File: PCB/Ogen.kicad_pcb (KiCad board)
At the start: 2 copper layers, 28 x 21.5 mm, 19 parts, among them J1 Input, U1 PMW3360DM-T2QU, U2 AP2127K-ADJ, U3 TXS0102DCU, U4 TXS0102DCU, U5 TXS0102DCU

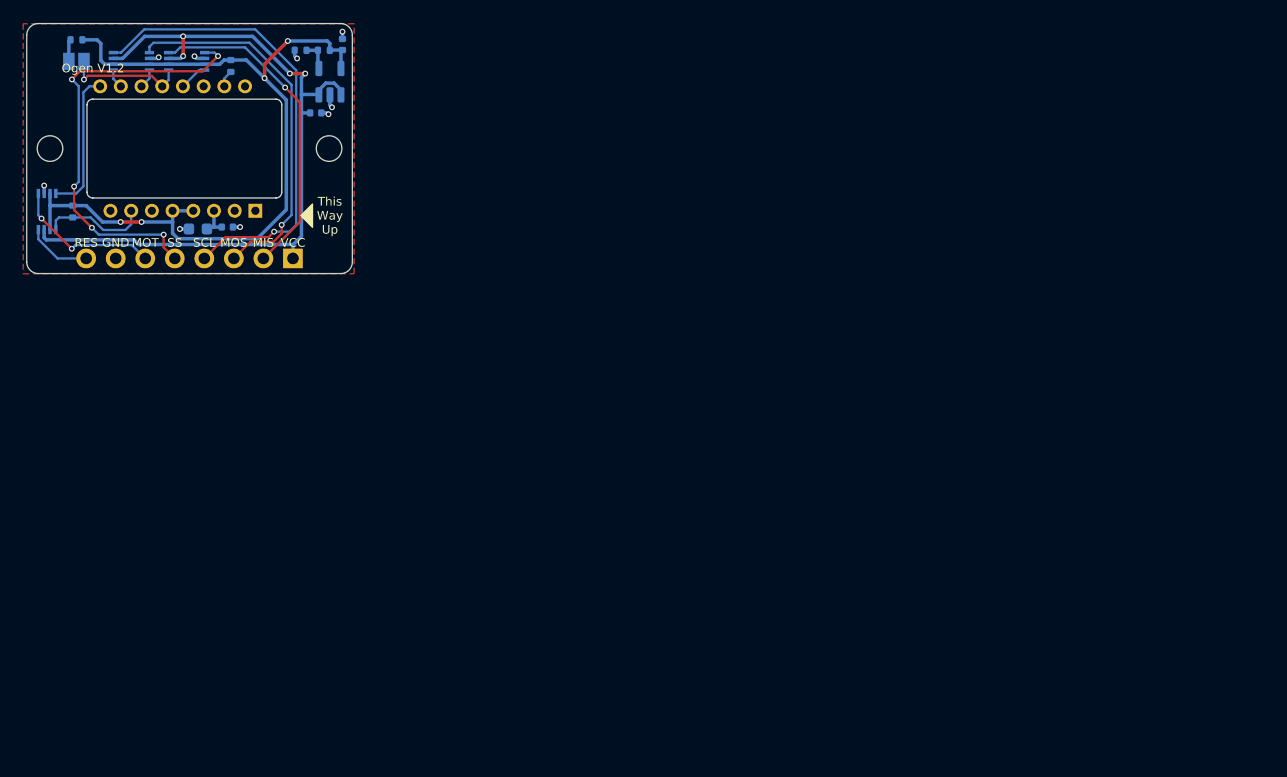
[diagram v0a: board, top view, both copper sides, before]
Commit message: 04/08/2023 update
Updated to V1.3. Changed all parts back to 0603. Stitched ground planes together. Removed MISO pullup jumper (MISO is pulled up by default now). Added metadata to schematic and PCB file. Changed location of production files for easier access.
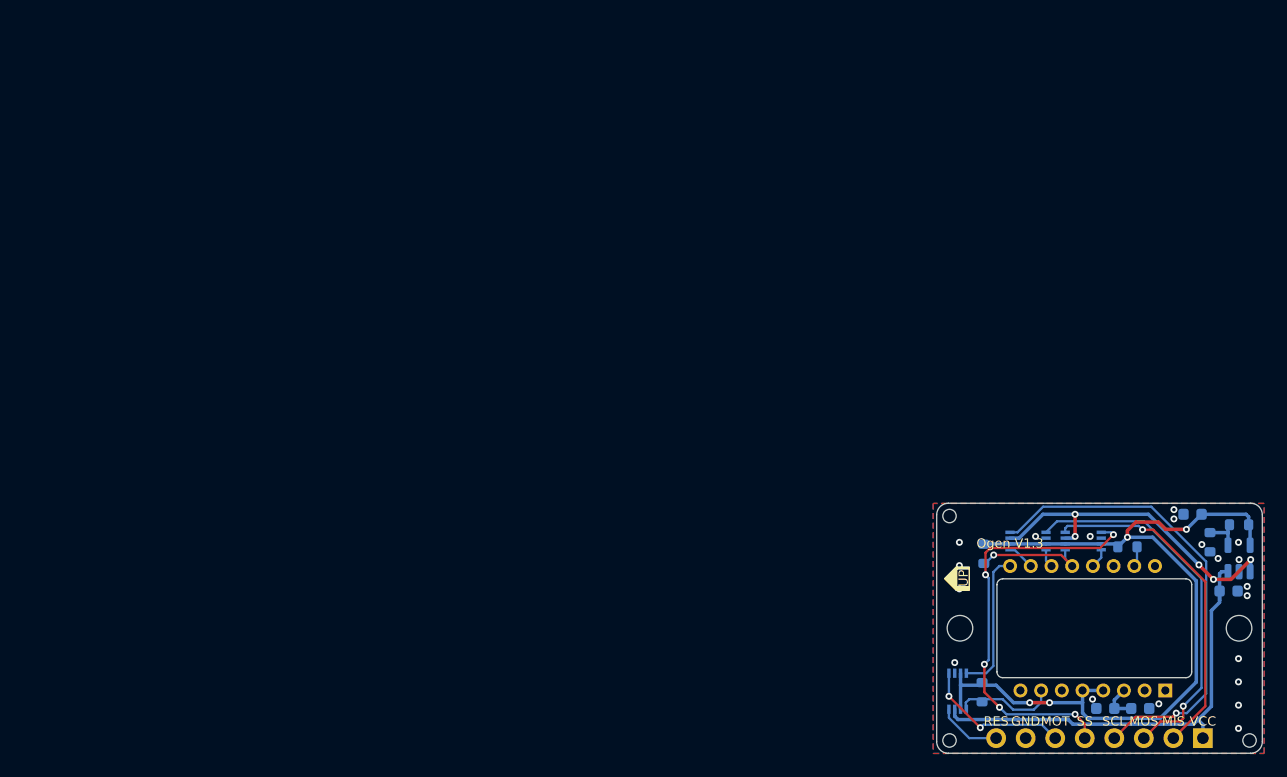
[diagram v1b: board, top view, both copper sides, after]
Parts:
- removed JP1: Jumper, Jumper:SolderJumper-2_P1.3mm_Open_Pad1.0x1.5mm
- added H3: Tooling Hole, Ogen:JLC Tooling Hole, F.Cu at (92.1, 55.4)
- added H4: Tooling Hole, Ogen:JLC Tooling Hole, F.Cu at (92.1, 74.7)
- added H5: Tooling Hole, Ogen:JLC Tooling Hole, F.Cu at (117.9, 74.7)
- C2, C3, C4: footprint Capacitor_SMD:C_0402_1005Metric -> Capacitor_SMD:C_0603_1608Metric
- R1, R2, R3, R4, R5: footprint Resistor_SMD:R_0402_1005Metric -> Resistor_SMD:R_0603_1608Metric
- U3, U4, U5: footprint Package_SO:VSSOP-8_2.3x2mm_P0.5mm -> Ogen:VSSOP-8_2.3x2mm_P0.5mm
- moved C1 90.9 mm to (108.5, 71.9), turned to 0 degrees
- moved R2 89.7 mm to (95.0, 58.6), turned to -90 degrees
- moved R4 88.9 mm to (114.5, 57.6), turned to -90 degrees
- moved A1 88.9 mm to (97.3, 55.8)
- moved R5 88.6 mm to (117.0, 56.1)
- moved C3 88.6 mm to (116.1, 61.8)
- moved U3 88.5 mm to (92.8, 70.4)
- moved H1 88.5 mm to (117.0, 65.0)
- moved H2 88.5 mm to (93.0, 65.0)
- moved J1 88.5 mm to (105.0, 74.5)
- moved U1 88.5 mm to (105.0, 65.0)
- moved R1 88.5 mm to (94.9, 70.5)
- moved U2 88.3 mm to (117.0, 59.0)
- moved R3 87.5 mm to (107.4, 58.0), turned to 180 degrees
- moved U4 87.4 mm to (98.8, 57.5)
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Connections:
- R2 pad 2: Net-(JP1-A) -> MISO
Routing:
- net GND: track 7.09 -> 0.00 mm, vias 9 -> 20
- net +2V: track 70.2 -> 72.9 mm
- net Net-(JP1-A): track 1.92 -> 0.00 mm
- net SS-H: track 37.8 -> 36.0 mm
- net VCC: track 65.9 -> 67.6 mm, vias 4 -> 5
- net MISO-H: track 28.1 -> 29.1 mm
- net Net-(U2-ADJ): track 2.58 -> 3.37 mm
- net SS: track 2.45 -> 1.70 mm
- net SCLK: track 1.67 -> 2.37 mm
- net MISO: track 10.4 -> 9.82 mm
- net Net-(U1-VDDPIX): track 2.76 -> 3.34 mm
- added copper zone on B.Cu, net GND
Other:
- board text added: "Ogen V1.3"
- board text added: "UP"
- board text removed: "MISO Pullup"
- board text removed: "Ogen V1.2"
- board text removed: "This Way Up"

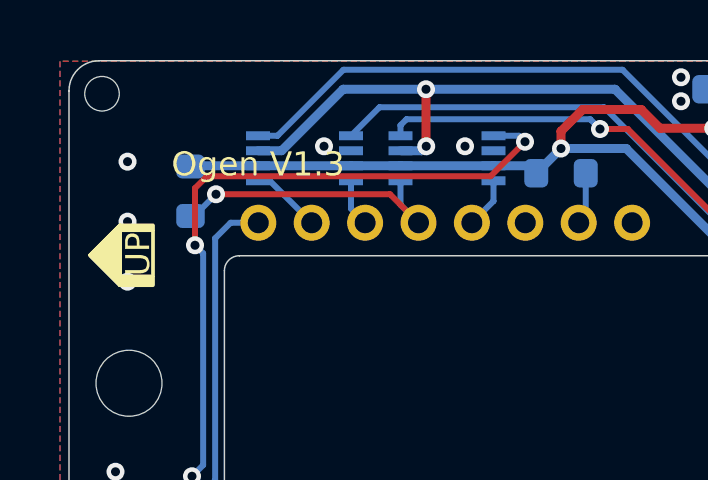
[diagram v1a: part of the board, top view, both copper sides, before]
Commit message: 18/09/2023 update
Updated to V1.4. Fixed .gitignore file. Changed LDO capacitors to 4u7 to match the one used in the PMW3360.
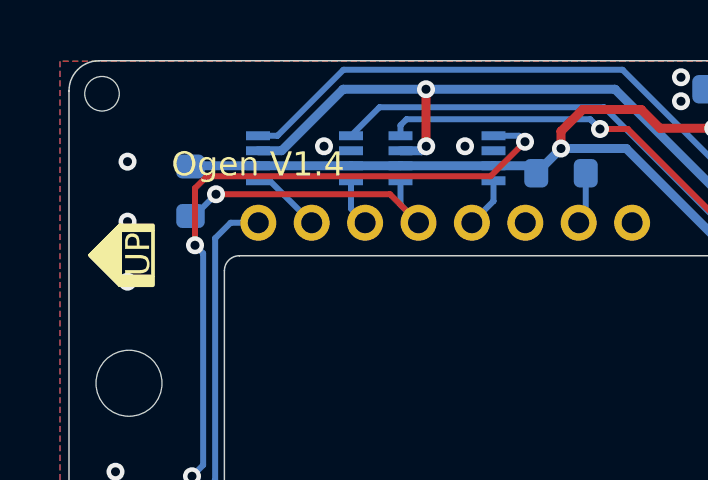
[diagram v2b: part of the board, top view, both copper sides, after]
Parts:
- C3, C4: value 1u -> 4u7
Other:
- board text added: "Ogen V1.4"
- board text removed: "Ogen V1.3"
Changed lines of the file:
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@@
   (title_block
     (title "Ogen PMW3360 Module")
-    (date "2023-08-04")
-    (rev "V1.3")
-    (company "Created by Ariamelon (https://github.com/Ariamelon/Ogen/tree/V1.3)")
+    (date "2023-09-18")
+    (rev "V1.4")
+    (company "Created by Ariamelon (https://github.com/Ariamelon/Ogen/tree/V1)")
     (comment 1 "Licensed under CC BY 4.0.")
   )
@@
     (property "Sheetfile" "Ogen.kicad_sch")
     (property "Sheetname" "")
+    (property "Voltage" "16V")
     (property "ki_description" "Unpolarized capacitor, small symbol")
     (property "ki_keywords" "capacitor cap")
@@
     (tags "capacitor")
     (property "Description" "0603 capacitor")
-    (property "LCSC" "C15849")
-    (property "Sheetfile" "Ogen.kicad_sch")
-    (property "Sheetname" "")
+    (property "LCSC" "C19666")
+    (property "Sheetfile" "Ogen.kicad_sch")
+    (property "Sheetname" "")
+    (property "Voltage" "16V")
     (property "ki_description" "Unpolarized capacitor, small symbol")
     (property "ki_keywords" "capacitor cap")
@@
         (effects (font (size 0.8 0.8) (thickness 0.1)) (justify mirror))
     )
-    (fp_text value "1u" (at 0 -1.43 180 unlocked) (layer "B.Fab")
+    (fp_text value "4u7" (at 0 -1.43 180 unlocked) (layer "B.Fab")
         (effects (font (size 1 1) (thickness 0.15)) (justify mirror))
     )
@@
     (tags "capacitor")
     (property "Description" "0603 capacitor")
-    (property "LCSC" "C15849")
-    (property "Sheetfile" "Ogen.kicad_sch")
-    (property "Sheetname" "")
+    (property "LCSC" "C19666")
+    (property "Sheetfile" "Ogen.kicad_sch")
+    (property "Sheetname" "")
+    (property "Voltage" "16V")
     (property "ki_description" "Unpolarized capacitor, small symbol")
     (property "ki_keywords" "capacitor cap")
@@
         (effects (font (size 0.8 0.8) (thickness 0.1)) (justify mirror))
     )
-    (fp_text value "1u" (at 0 -1.43 unlocked) (layer "B.Fab")
+    (fp_text value "4u7" (at 0 -1.43 unlocked) (layer "B.Fab")
         (effects (font (size 1 1) (thickness 0.15)) (justify mirror))
     )
@@
     (effects (font (size 0.8 0.8) (thickness 0.1)))
   )
-  (gr_text "Ogen V1.3" (at 97.3 57.7) (layer "F.SilkS")
+  (gr_text "Ogen V1.4" (at 97.3 57.7) (layer "F.SilkS")
     (effects (font (size 0.8 0.8) (thickness 0.1)))
   )

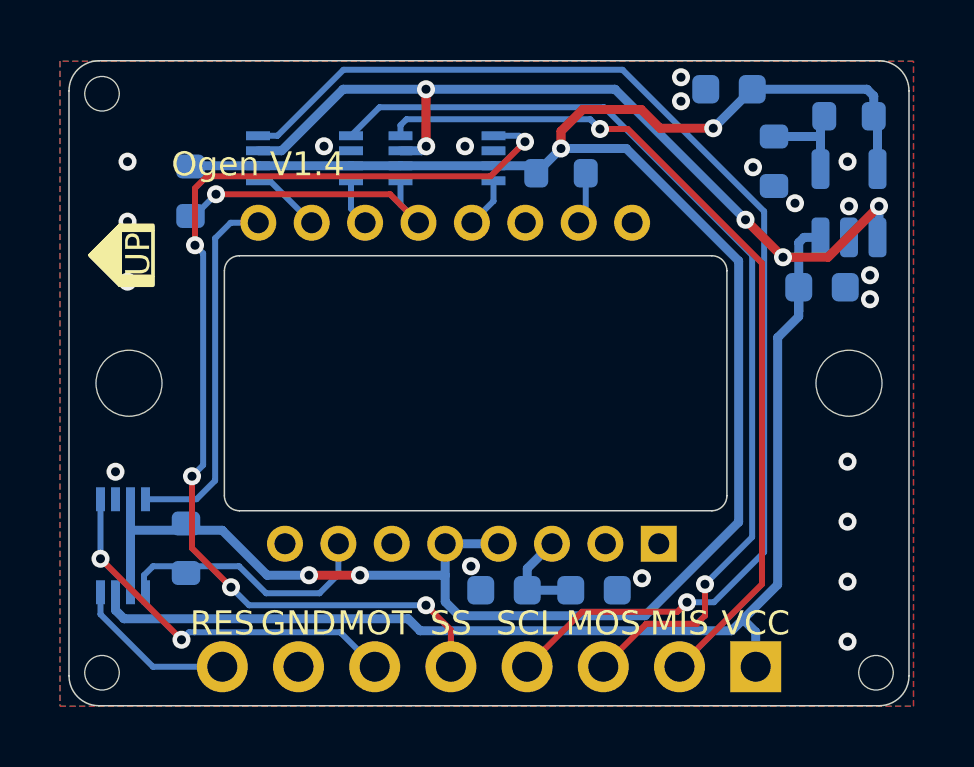
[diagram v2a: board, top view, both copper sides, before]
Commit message: V1.5 update
Changed LDO to XC6206P202MR. Unified libraries with master library.
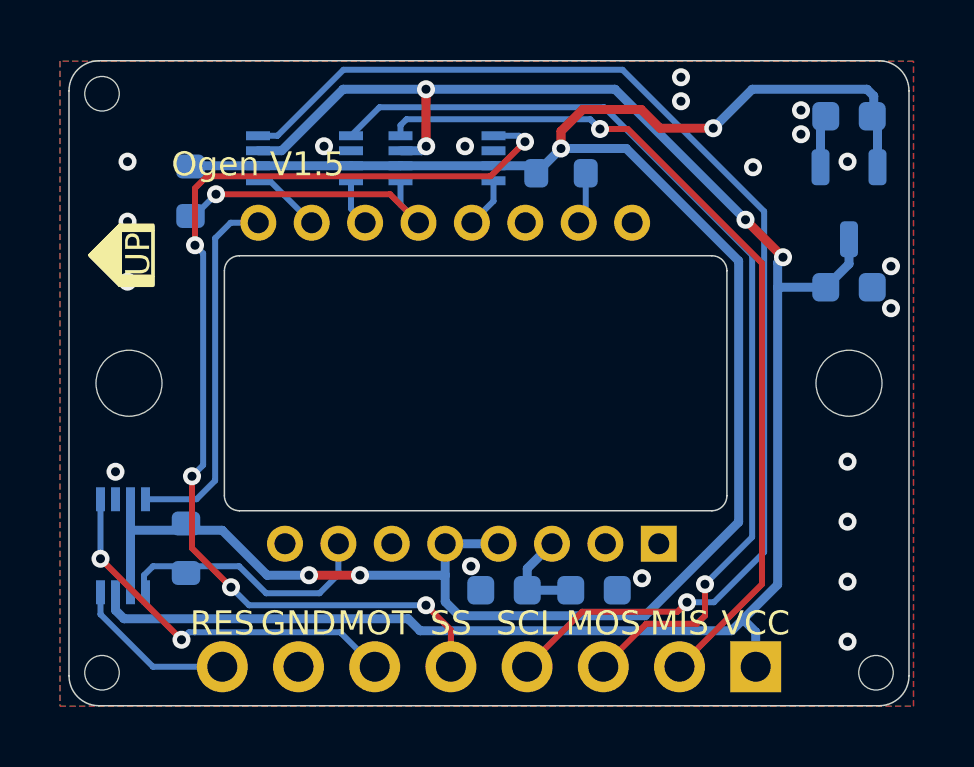
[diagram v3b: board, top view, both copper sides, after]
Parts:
- removed R4: 10k, Resistor_SMD:R_0603_1608Metric
- removed R5: 15k, Resistor_SMD:R_0603_1608Metric
- U1: value PMW3360DM-T2QU -> PMW3360DM-T2QU_1
- U2: value AP2127K-ADJ -> XC6206P202MR; footprint Package_TO_SOT_SMD:SOT-23-5 -> Ariamelon-Package:SOT-23-3
- moved C4 4.10 mm to (117.0, 56.1)
- moved C3 0.90 mm to (117.0, 61.8)
- turned U2 to -90 degrees
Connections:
- U2 pad 1: VCC -> GND
- U2 pad 2: GND -> +2V
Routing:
- net VCC: track 67.6 -> 63.4 mm, vias 5 -> 4
- net Net-(U2-ADJ): track 3.37 -> 0.00 mm
- net GND: track 0.00 -> 1.81 mm
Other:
- board text added: "Ogen V1.5"
- board text removed: "Ogen V1.4"
